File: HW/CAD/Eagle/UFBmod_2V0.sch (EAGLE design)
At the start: 75 parts, among them U301 MAX5217, U401 AT86RF215-ZU, U411 ASVTX-13-D-26.000MHZ-I05-T, U511 PE4259, U521 RFX1010, U581 B39871B3440U410, X1 TTE_EN11-HSM, X591 ANTENNATINY, X595 ANTENNATINY, X711 MOLEX 105017-0001, X721 PHOENIX_1990067_1X8X2MM50_PTS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, X722 PHOENIX_1990067_1X8X2MM50_PTS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, X723 PHOENIX_1990067_1X8X2MM50_PTS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

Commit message: HW_2V0 - HW/CAD/Eagle - board size changed
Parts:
- removed C1, C2, C3, C403, C404, C521, C531, C532, C711: 1nF, df4iah_rcl:C-EUC0402
- removed C311, C312, C406, C407, C408, C511: 100nF, df4iah_rcl:C-EUC0402
- removed C321, C401: 1uF, df4iah_rcl:C-EUC0402
- removed C411, C412, C551, C552, C553: 10nF, df4iah_rcl:C-EUC0402
- removed C413: 56pF, df4iah_rcl:C-EUC0402
- removed C591, C595, C597: 0pF, df4iah_rcl:C-EUC0402
- removed C601: 10uF, df4iah_rcl:C-EUC0603
- removed C621: 22uF, df4iah_rcl:C-EUC0603
- removed D1: ASMT-YTB7-0AA02_RGB, df4iah_led:ASMT-YTB7-0AA02_RGB
- removed H2311, H2321, H2331, H2341: MOUNT-PAD-ROUND2.8, df4iah_holes:MOUNT-PAD-ROUND2.8
- removed L1: 6.8nH, df4iah_rcl:L-EUL0603
- removed L401, L402, L403, L404: 300R, df4iah_rcl:R-EU_R1206
- removed L421: MURATA DXW21HN5011BL, df4iah_balun:DXW21HN5011BL
- removed L422: Johanson 2450BL15B050E, df4iah_balun:2450BL15B050
- removed L521: 2.7nH, df4iah_rcl:L-EUL0603
- removed L592, L596: 0nH, df4iah_rcl:L-EUL0603
- removed L611: 440nH, df4iah_rcl:L-EUL1812
- removed PF711: 1.1A/2.2A, rcl:R-EU_M1206
- removed R1, R3: 820R, df4iah_rcl:R-EU_R0402
- removed R2: 1kR, df4iah_rcl:R-EU_R0402
- removed R321: 100kR, df4iah_rcl:R-EU_R0402
- removed R4, R5, R6, R7: 10kR, df4iah_rcl:R-EU_R0402
- removed R413, R521: 100R, df4iah_rcl:R-EU_R0402
- removed R711: 330kR, df4iah_rcl:R-EU_R0402
- removed U301: MAX5217, df4iah_dac:MAX5217
- removed U401: AT86RF215-ZU, df4iah_rf:AT86RF215
- removed U411: ASVTX-13-D-26.000MHZ-I05-T, df4iah_osc:ASVTX-13-D
- removed U511: PE4259, df4iah_rf:PE4259
- removed U521: RFX1010, df4iah_rf:RFX1010
- removed U581: B39871B3440U410, df4iah_rf:B3440
- removed X1: TTE_EN11-HSM, df4iah_switch:TTE_EN11-HSM
- removed X591, X595: ANTENNATINY, _c2h:ANTENNATINY
- removed X711: MOLEX 105017-0001, df4iah_connector:USB_MICRO-B_MOLEX
- removed X721, X722, X723: PHOENIX_1990067_1X8X2MM50_PTSA-0-5, df4iah_connector:PHOENIX_1990067_1X8X2MM50_PTSA-0-5
- added C0501, C0611, C0612, C0706, C0707, C0708, C0811: 100nF, df4iah_rcl:C-EUC0402
- added C0511, C0512, C0621, C0701: 1uF, df4iah_rcl:C-EUC0402
- added C0703, C0704, C0821, C0831, C0832, C1011, C1012, C1013, C1211: 1nF, df4iah_rcl:C-EUC0402
- added C0711, C0712, C0851, C0852, C0853: 10nF, df4iah_rcl:C-EUC0402
- added C0713: 56pF, df4iah_rcl:C-EUC0402
- added C0891, C0895, C0897: 0pF, df4iah_rcl:C-EUC0402
- added C1121: 22uF, df4iah_rcl:C-EUC0603
- added D1021: ASMT-YTB7-0AA02_RGB, df4iah_led:ASMT-YTB7-0AA02_RGB
- added D1111, D1112: CRS08, df4iah_diode:CRS08
- added H1311, H1312, H1313, H1314, HB_351, HB_352, HB_353, HB_354: MOUNT-PAD-ROUND3.2, df4iah_holes:MOUNT-PAD-ROUND3.2
- added L0701, L0702, L0703, L0704: 300R, df4iah_rcl:R-EU_R1206
- added L0721: MURATA DXW21HN5011BL, df4iah_balun:DXW21HN5011BL
- added L0722: Johanson 2450BL15B050E, df4iah_balun:2450BL15B050
- added L0821: 2.7nH, df4iah_rcl:L-EUL0603
- added L0853: 6.8nH, df4iah_rcl:L-EUL0603
- added L0892, L0896: 0nH, df4iah_rcl:L-EUL0603
- added L1101: 440nH, df4iah_rcl:L-EUL1812
- added PF1211: 1.1A/2.2A, rcl:R-EU_M1206
- added R0531: 220kR, df4iah_rcl:R-EU_R0402
- added R0551: 1.5kR, df4iah_rcl:R-EU_R0402
- added R0552: 2.0kR, df4iah_rcl:R-EU_R0402
- added R0553: 27R, df4iah_rcl:R-EU_R0603
- added R0621: 100kR, df4iah_rcl:R-EU_R0402
- added R0713, R0821: 100R, df4iah_rcl:R-EU_R0402
- added R0822, R0861, R0862, R0863: 10kR, df4iah_rcl:R-EU_R0402
- added R1021, R1023: 820R, df4iah_rcl:R-EU_R0402
- added R1022: 1kR, df4iah_rcl:R-EU_R0402
- added R1211: 330kR, df4iah_rcl:R-EU_R0402
- added T0551: MMBT2222, transistor:BC846
- added U0501: MIDAS_MCCOG21605B6W-FPTLWI, df4iah_lcd:MIDAS_MCCOG21605B6W-FPTLWI
- added U0601: MAX5217, df4iah_dac:MAX5217
- added U0701: AT86RF215-ZU, df4iah_rf:AT86RF215
- added U0711: ASVTX-13-D-26.000MHZ-I05-T, df4iah_osc:ASVTX-13-D
- added U0811: PE4259, df4iah_rf:PE4259
- added U0821: RFX1010, df4iah_rf:RFX1010
- added U0881: B39871B3440U410, df4iah_rf:B3440
- added X0891, X0895: ANTENNATINY, _c2h:ANTENNATINY
- added X1011: TTE_EN11-HSM, df4iah_switch:TTE_EN11-HSM
- added X1211: MOLEX 105017-0001, df4iah_connector:USB_MICRO-B_MOLEX
- added X1221, X1222, X1223: PHOENIX_1990067_1X8X2MM50_PTSA-0-5, df4iah_connector:PHOENIX_1990067_1X8X2MM50_PTSA-0-5
- renumbered R211 to R0411, R212 to R0412
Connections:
- removed net +5V: C601.1, PF711.1
- new net +5V_USB: D1112.A, PF1211.1
- new net LCD_BL_K: T0551.C, U0501.K_BL
- new net LCD_BL_PWM: R0552.2
- new net LCD_CAP1N: C0511.2
- new net LCD_CAP1P: C0511.1
- new net LCD_NRST: R0531.2
- new net LCD_VOUT: C0512.1
- new net LED_B_B: R0551.2, R0552.1, T0551.B
- new net LED_B_E: R0553.2, T0551.E
- new net VIN_PWR: D1111.A
- new net VIN_REG: D1111.C, D1112.C
- net +3V3: now also C0501.1, C0611.1, C0612.1, C0701.1, C0711.1, C0811.1, C0851.1, C0852.1, C0853.1, C1121.1, L0703.1, L0704.1, L0853.1, L1101.1, U0501.A_BL, U0601.!AUX, U0601.REF, U0601.VDD, U0711.VCC_3V3, U0811.VDD_!CTRL, U0821.VDD1, U0821.VDD2; no longer C311.1, C312.1, C401.1, C411.1, C511.1, C551.1, C552.1, C553.1, C621.1, L1.1, L403.1, L404.1, L611.1, U301.!AUX, U301.REF, U301.VDD, U411.VCC_3V3, U511.VDD_!CTRL, U521.VDD1, U521.VDD2
- net 26MHZ_DAC_OUT: now also R0621.1, U0601.OUT; no longer R321.1, U301.OUT
- net ANT09: now also L0892.2, X0891.SIGNAL; no longer L592.2, X591.SIGNAL
- net ANT09_MATCH: now also C0891.1, L0892.1, U0881.OUT; no longer C591.1, L592.1, U581.OUT
- net ANT24: now also C0897.1, L0896.2, X0895.SIGNAL; no longer C597.1, L596.2, X595.SIGNAL
- net FE09_ANT: now also U0821.ANT, U0881.IN; no longer U521.ANT, U581.IN
- net FE09_RX: now also C0832.1, U0821.RX; no longer C532.1, U521.RX
- net FE09_TX: now also C0831.1, U0821.TX; no longer C531.1, U521.TX
- net FPGA_I2C_SCL: now also U0601.SCL; no longer U301.SCL
- net FPGA_I2C_SDA: now also U0601.SDA; no longer U301.SDA
- net FPGA_RFX_DET: now also R0821.2; no longer R521.2
- net FPGA_RFX_MODE: now also R0861.1; no longer R7.1
- net FPGA_TRX_CLKO: now also C0713.1, R0713.1; no longer C413.1, R413.1
- net GND: now also C0501.2, C0512.2, C0611.2, C0612.2, C0621.2, C0701.2, C0711.2, C0713.2, C0811.2, C0851.2, C0852.2, C0853.2, C0891.2, C0895.2, C0897.2, C1011.2, C1012.2, C1013.2, C1121.2, C1211.1, D1021.BC, D1021.GC, D1021.RC, H1311.MOUNT, H1312.MOUNT, H1313.MOUNT, H1314.MOUNT, HB_351.MOUNT, HB_352.MOUNT, HB_353.MOUNT, HB_354.MOUNT, JB1.GND@1, JB1.GND@19, JB1.GND@25, JB1.GND@30, JB1.GND@33, JB1.GND@43, JB1.GND@53, JB1.GND@54, JB1.GND@63, JB1.GND@64, JB1.GND@7, JB1.GND@73, JB1.GND@74, JB1.GND@83, JB1.GND@89, JB2.GND@19, JB2.GND@29, JB2.GND@39, JB2.GND@40, JB2.GND@49, JB2.GND@50, JB2.GND@59, JB2.GND@60, JB2.GND@69, JB2.GND@70, JB2.GND@79, JB2.GND@80, JB2.GND@89, JB3.GND@11, JB3.GND@17, JB3.GND@18, JB3.GND@23, JB3.GND@24, JB3.GND@29, JB3.GND@30, JB3.GND@35, JB3.GND@36, JB3.GND@45, JB3.GND@46, JB3.GND@5, JB3.GND@6, L0701.1, L0702.1, L0721.COM, L0722.COM, L0722.G_N_D, L0821.2, R0531.1, R0551.1, R0553.1, R0822.1, R1211.1, U0601.ADDR, U0601.GND, U0711.GND, U0811.GND, U0821.VSS@17, U0821.VSS@4, U0821.VSS@8, U0881.GROUND, X0891.GND@0, X0891.GND@1, X0891.GND@2, X0891.GND@3, X0895.GND@0, X0895.GND@1, X0895.GND@2, X0895.GND@3, X1011.C, X1011.D, X1211.GND; no longer C1.2, C2.2, C3.2, C311.2, C312.2, C321.2, C401.2, C411.2, C413.2, C511.2, C551.2, C552.2, C553.2, C591.2, C595.2, C597.2, C601.2, C621.2, C711.1, D1.BC, D1.GC, D1.RC, H2311.MOUNT, H2321.MOUNT, H2331.MOUNT, H2341.MOUNT, L401.1, L402.1, L421.COM, L422.COM, L422.G_N_D, L521.2, R6.1, R711.1, U301.ADDR, U301.GND, U411.GND, U511.GND, U521.VSS@17, U521.VSS@4, U521.VSS@8, U581.GROUND, X1.C, X1.D, X591.GND@0, X591.GND@1, X591.GND@2, X591.GND@3, X595.GND@0, X595.GND@1, X595.GND@2, X595.GND@3, X711.GND
- net LED_B1: now also R1023.2; no longer R3.2
- net LED_B_R1: now also D1021.BA, R1023.1; no longer D1.BA, R3.1
- net LED_G1: now also R1022.2; no longer R2.2
- net LED_G_R1: now also D1021.GA, R1022.1; no longer D1.GA, R2.1
- net LED_R1: now also R1021.2; no longer R1.2
- net LED_R_R1: now also D1021.RA, R1021.1; no longer D1.RA, R1.1
- net PE09_RF1: now also C0831.2, U0811.RF1; no longer C531.2, U511.RF1
- net PE09_RF2: now also C0832.2, U0811.RF2; no longer C532.2, U511.RF2
- net PE09_RFC: now also C0821.1, U0811.RFC; no longer C521.1, U511.RFC
- net PMIC3V3_SW: now also L1101.2; no longer L611.2
- net RFX_DET: now also R0821.1, R0822.2, U0821.DET; no longer R521.1, R6.2, U521.DET
- net RFX_IND: now also L0821.1, U0821.IND; no longer L521.1, U521.IND
- net RFX_MODE: now also R0861.2, U0821.MODE; no longer R7.2, U521.MODE
- net RFX_RXEN: now also R0862.2, U0821.RXEN; no longer R4.2, U521.RXEN
- net RFX_TXEN: now also R0863.2, U0821.TXEN; no longer R5.2, U521.TXEN
- net RFX_VDD3: now also L0853.2, U0821.VDD3; no longer L1.2, U521.VDD3
- net ROT_I_R: now also C1011.1, X1011.A; no longer C1.1, X1.A
- net ROT_P: now also C1013.1, X1011.E; no longer C3.1, X1.E
- net ROT_Q_R: now also C1012.1, X1011.B; no longer C2.1, X1.B
- net TRX_AVDD0: now also C0707.2, U0701.AVDD0; no longer C407.2, U401.AVDD0
- net TRX_AVDD1: now also C0708.2, U0701.AVDD1; no longer C408.2, U401.AVDD1
- net TRX_AVSS: now also C0704.2, C0707.1, C0708.1, L0701.2, U0701.AVSS, U0701.XTAL2; no longer C404.2, C407.1, C408.1, L401.2, U401.AVSS, U401.XTAL2
- net TRX_CLKO: now also R0713.2, U0701.CLKO; no longer R413.2, U401.CLKO
- net TRX_DEVDD: now also C0703.1, L0703.2, U0701.DEVDD; no longer C403.1, L403.2, U401.DEVDD
- net TRX_DVDD: now also C0706.2, U0701.DVDD; no longer C406.2, U401.DVDD
- net TRX_DVSS: now also C0703.2, C0706.1, L0702.2, U0701.DVSS; no longer C403.2, C406.1, L402.2, U401.DVSS
- net TRX_EVDD: now also C0704.1, L0704.2, U0701.EVDD; no longer C404.1, L404.2, U401.EVDD
- net TRX_FEA09: now also R0863.1, U0701.FEA09, U0811.CTRL; no longer R5.1, U401.FEA09, U511.CTRL
- net TRX_FEA24: now also U0701.FEA24; no longer U401.FEA24
- net TRX_FEB09: now also R0862.1, U0701.FEB09; no longer R4.1, U401.FEB09
- net TRX_FEB24: now also U0701.FEB24; no longer U401.FEB24
- net TRX_IRQ: now also U0701.IRQ; no longer U401.IRQ
- net TRX_MISO: now also U0701.MISO; no longer U401.MISO
- net TRX_MOSI: now also U0701.MOSI; no longer U401.MOSI
- net TRX_RF09: now also C0821.2, L0721.UB; no longer C521.2, L421.UB
- net TRX_RF09_N: now also L0721.B2, U0701.RF09N; no longer L421.B2, U401.RF09N
- net TRX_RF09_P: now also L0721.B1, U0701.RF09P; no longer L421.B1, U401.RF09P
- net TRX_RF24: now also C0895.1, L0722.UB, L0896.1; no longer C595.1, L422.UB, L596.1
- net TRX_RF24_N: now also L0722.B2, U0701.RF24N; no longer L422.B2, U401.RF24N
- net TRX_RF24_P: now also L0722.B1, U0701.RF24P; no longer L422.B1, U401.RF24P
- net TRX_RSTN: now also U0701.RSTN; no longer U401.RSTN
- net TRX_RXCLK_N: now also U0701.RXCLKN; no longer U401.RXCLKN
- net TRX_RXCLK_P: now also U0701.RXCLKP; no longer U401.RXCLKP
- net TRX_RXD09_N: now also U0701.RXD09N; no longer U401.RXD09N
- net TRX_RXD09_P: now also U0701.RXD09P; no longer U401.RXD09P
- net TRX_RXD24_N: now also U0701.RXD24N; no longer U401.RXD24N
- net TRX_RXD24_P: now also U0701.RXD24P; no longer U401.RXD24P
- net TRX_SCLK: now also U0701.SCLK; no longer U401.SCLK
- net TRX_SELN: now also U0701.SELN; no longer U401.SELN
- net TRX_TCXO: now also C0712.2, U0701.TCXO; no longer C412.2, U401.TCXO
- net TRX_TXCLK_N: now also U0701.TXCLKN; no longer U401.TXCLKN
- net TRX_TXCLK_P: now also U0701.TXCLKP; no longer U401.TXCLKP
- net TRX_TXD_N: now also U0701.TXDN; no longer U401.TXDN
- net TRX_TXD_P: now also U0701.TXDP; no longer U401.TXDP
- net USB_SHIELD: now also C1211.2, R1211.2, X1211.SHIELD; no longer C711.2, R711.2, X711.SHIELD
- net USB_VBUS: now also PF1211.2, X1211.J_VUSB; no longer PF711.2, X711.J_VUSB
- net VCTCXO_OUT: now also C0712.1, U0711.OUT; no longer C412.1, U411.OUT
- net VCTCXO_VC: now also C0621.1, R0621.2, U0711.VC; no longer C321.1, R321.2, U411.VC
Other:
- note added: "Addr Device 0x38 DAC 0x3D LCD"
- note added: "I2C LCD module I2C addr: 0x3D"
- note added: "I2C: LCD"
- note added: "LCD_NRST"
- note added: "Module mount pads"
- note added: "X0891"
- note added: "X0895"
- note removed: "Addr Device 0x38 DAC"
- note removed: "X591"
- note removed: "X595"

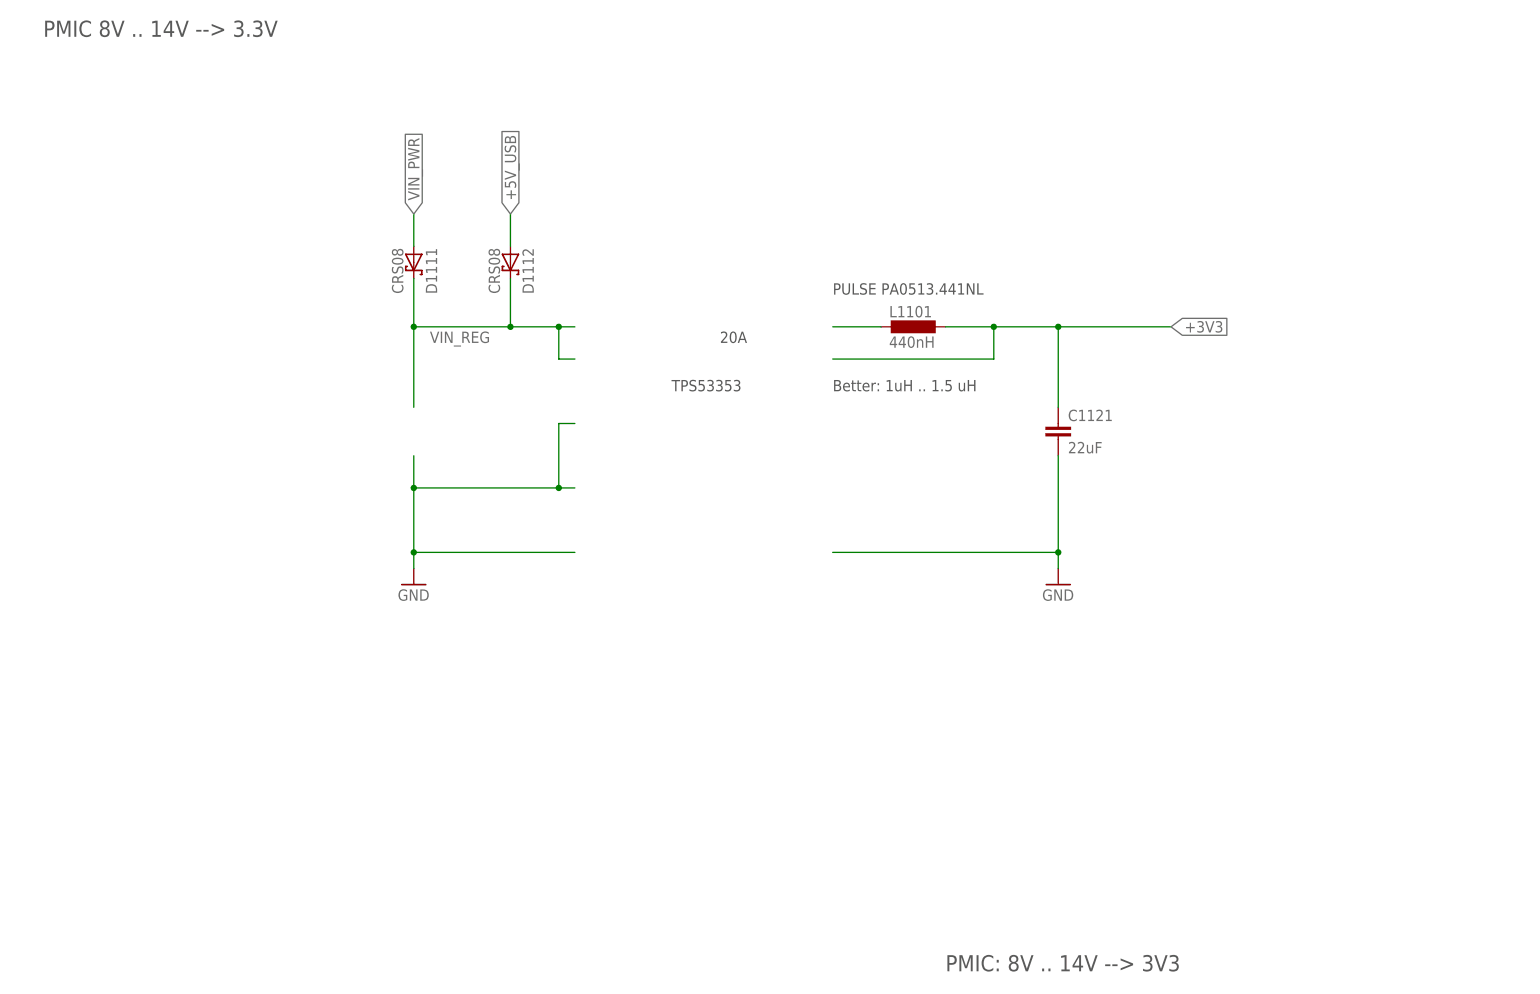
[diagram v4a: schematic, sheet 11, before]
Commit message: HW_2V0 - HW/CAD/Eagle - TPS53353 added
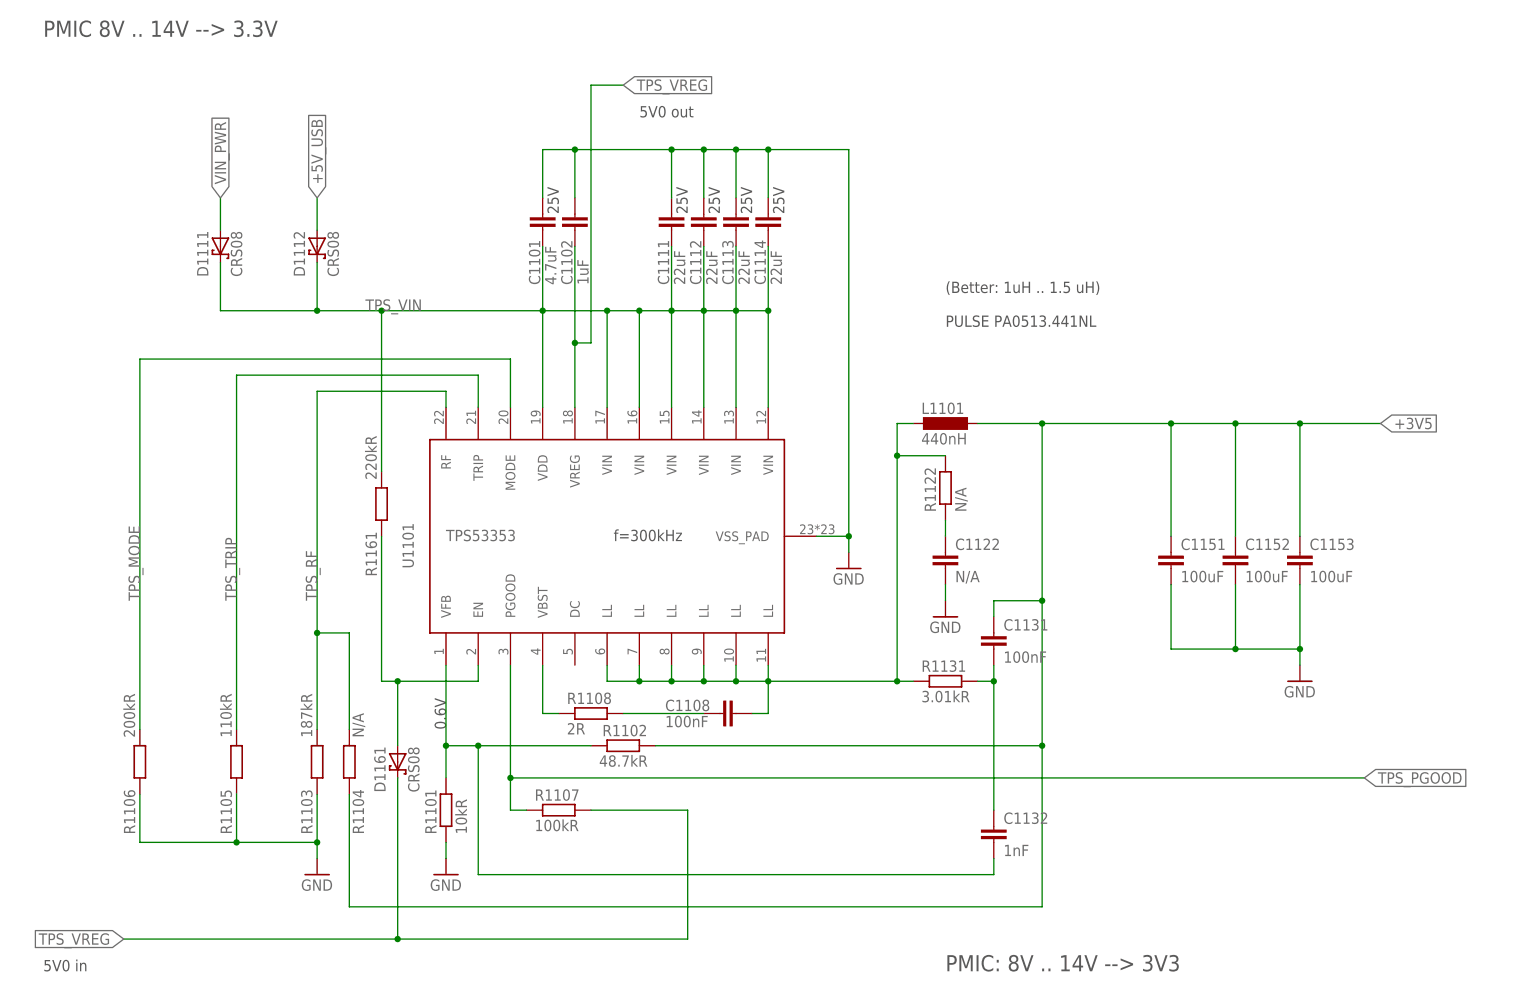
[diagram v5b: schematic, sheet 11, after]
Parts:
- removed C1121: 22uF, df4iah_rcl:C-EUC0603
- added C1101: 4.7uF, df4iah_rcl:C-EUC0805
- added C1102: 1uF, df4iah_rcl:C-EUC0402
- added C1108: 100nF, df4iah_rcl:C-EUC0805
- added C1111, C1112, C1113, C1114: 22uF, df4iah_rcl:C-EUC0805
- added C1122: N/A, df4iah_rcl:C-EUC0805
- added C1131: 100nF, df4iah_rcl:C-EUC0402
- added C1132: 1nF, df4iah_rcl:C-EUC0402
- added C1151, C1152, C1153: 100uF, df4iah_rcl:C-EUC0805
- added D1161: CRS08, df4iah_diode:CRS08
- added R1101: 10kR, df4iah_rcl:R-EU_R0402
- added R1102: 48.7kR, df4iah_rcl:R-EU_R0402
- added R1103: 187kR, df4iah_rcl:R-EU_R0402
- added R1104: N/A, df4iah_rcl:R-EU_R0402
- added R1105: 110kR, df4iah_rcl:R-EU_R0402
- added R1106: 200kR, df4iah_rcl:R-EU_R0402
- added R1107: 100kR, df4iah_rcl:R-EU_R0402
- added R1108: 2R, df4iah_rcl:R-EU_R0805
- added R1122: N/A, df4iah_rcl:R-EU_R0805
- added R1131: 3.01kR, df4iah_rcl:R-EU_R0402
- added R1161: 220kR, df4iah_rcl:R-EU_R0402
- added U1101: TPS53353, df4iah_powersupply:TPS53353
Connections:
- removed net PMIC3V3_SW: L1101.2
- removed net VIN_REG: D1111.C, D1112.C
- new net +3V5: C1131.1, C1151.1, C1152.1, C1153.1, L1101.1, R1102.2, R1104.1
- new net TPS_COR: C1131.2, C1132.1, R1131.2
- new net TPS_EN: D1161.A, R1161.1, U1101.EN
- new net TPS_LL: C1108.1, L1101.2, R1122.2, R1131.1, U1101.LL@10, U1101.LL@11, U1101.LL@6, U1101.LL@7, U1101.LL@8, U1101.LL@9
- new net TPS_LL_RC: C1122.1, R1122.1
- new net TPS_MODE: R1106.2, U1101.MODE
- new net TPS_PGOOD: R1107.1, U1101.PGOOD
- new net TPS_RF: R1103.2, R1104.2, U1101.RF
- new net TPS_TRIP: R1105.2, U1101.TRIP
- new net TPS_VBST: R1108.1, U1101.VBST
- new net TPS_VBST_R: C1108.2, R1108.2
- new net TPS_VFB: C1132.2, R1101.2, R1102.1, U1101.VFB
- new net TPS_VIN: C1101.2, C1111.2, C1112.2, C1113.2, C1114.2, D1111.C, D1112.C, R1161.2, U1101.VDD, U1101.VIN@12, U1101.VIN@13, U1101.VIN@14, U1101.VIN@15, U1101.VIN@16, U1101.VIN@17
- new net TPS_VREG: C1102.2, D1161.C, R1107.2, U1101.VREG
- net +3V3: no longer C1121.1, L1101.1
- net GND: now also C1101.1, C1102.1, C1111.1, C1112.1, C1113.1, C1114.1, C1122.2, C1151.2, C1152.2, C1153.2, R1101.1, R1103.1, R1105.1, R1106.1, U1101.VSS_PAD; no longer C1121.2
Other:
- note added: "(Better: 1uH .. 1.5 uH)"
- note added: "0.6V"
- note added: "25V"
- note added: "5V0 in"
- note added: "5V0 out"
- note added: "f=300kHz"
- note removed: "20A"
- note removed: "Better: 1uH .. 1.5 uH"
- note removed: "TPS53353"
- moved on the sheet: D1111, D1112, L1101

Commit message: HW_2V0 - HW/CAD/Eagle - work of the day
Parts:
- removed C1211: 1nF, df4iah_rcl:C-EUC0402
- removed H1311, H1312, H1313, H1314: MOUNT-PAD-ROUND3.2, df4iah_holes:MOUNT-PAD-ROUND3.2
- removed PF1211: 1.1A/2.2A, rcl:R-EU_M1206
- removed R1211: 330kR, df4iah_rcl:R-EU_R0402
- removed X1211: MOLEX 105017-0001, df4iah_connector:USB_MICRO-B_MOLEX
- removed X1221, X1222, X1223: PHOENIX_1990067_1X8X2MM50_PTSA-0-5, df4iah_connector:PHOENIX_1990067_1X8X2MM50_PTSA-0-5
- added C1201, C1221: 10uF, df4iah_rcl:C-EUC0603
- added C1311: 1nF, df4iah_rcl:C-EUC0402
- added H1411, H1412, H1413, H1414: MOUNT-PAD-ROUND3.2, df4iah_holes:MOUNT-PAD-ROUND3.2
- added L1211: 4.7uH, df4iah_rcl:L-EUL2520
- added PF1311: 1.1A/2.2A, rcl:R-EU_M1206
- added R0001, R0002, R0003, R0532: 1kR, df4iah_rcl:R-EU_R0402
- added R0211: 0R, df4iah_rcl:R-EU_R0402
- added R0212: N/A, df4iah_rcl:R-EU_R0402
- added R1311: 330kR, df4iah_rcl:R-EU_R0402
- added U1211: TPS62745DSSR, df4iah_powersupply:TPS62745
- added X1311: MOLEX 105017-0001, df4iah_connector:USB_MICRO-B_MOLEX
- added X1321, X1322, X1323: PHOENIX_1990067_1X8X2MM50_PTSA-0-5, df4iah_connector:PHOENIX_1990067_1X8X2MM50_PTSA-0-5
- C1011, C1012, C1013: value 1nF -> 100nF
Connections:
- net LCD_BL_PWM renamed FPGA_LCD_BL_PWM
- net LED_B1 renamed FPGA_LED_RGB_BLUE
- net LED_B_B renamed LCD_BL_B
- net LED_B_R1 renamed LED_RGB_BLUE
- net LED_G1 renamed FPGA_LED_RGB_GREEN
- net LED_G_R1 renamed LED_RGB_GREEN
- net LED_R1 renamed FPGA_LED_RGB_RED
- net LED_R_R1 renamed LED_RGB_RED
- removed net ROT_I_R: C1011.1, X1011.A
- removed net ROT_Q_R: C1012.1, X1011.B
- new net +1V5: JB2.U1V5@20
- new net +1V8: JB1.U1V8@40, R0212.1
- new net +2V5: C1221.1, L1211.1, R0211.1, U1211.VOUT
- new net FPGA_ETH_RD_N: JB1.ETH_RD_N
- new net FPGA_ETH_RD_P: JB1.ETH_RD_P
- new net FPGA_ETH_TD_N: JB1.ETH_TD_N
- new net FPGA_ETH_TD_P: JB1.ETH_TD_P
- new net FPGA_LCD_NRST: R0532.1
- new net FPGA_ROT_I: R0001.2
- new net FPGA_ROT_P: R0003.2
- new net FPGA_ROT_Q: R0002.2
- new net PMIC3V3_SW: L1211.2, U1211.SW
- new net ROT_I: C1011.1, R0001.1, X1011.A
- new net ROT_Q: C1012.1, R0002.1, X1011.B
- new net VCCIO13: JB2.VCCIO13@2, JB2.VCCIO13@4, R0211.2, R0212.2
- net +3V3: now also JB1.U3V3@13, JB1.VCCIO16@10, JB1.VCCIO16@12, JB2.U3V3@11, JB2.U3V3@9, JB2.VCCIO15@10, JB2.VCCIO15@8, U0501.VDD
- net +3V5: now also C1201.1, JB1.U3V3IN@14, JB1.U3V3IN@16, JB1.VIN@2, JB1.VIN@4, JB1.VIN@6, JB2.VIN@1, JB2.VIN@3, JB2.VIN@5, JB2.VIN@7, U1211.EN, U1211.VIN, U1211.VSEL1, U1211.VSEL2, U1211.VSEL3
- net +5V_USB: now also PF1311.1; no longer PF1211.1
- net FPGA_I2C_SCL: now also U0501.SCL
- net FPGA_I2C_SDA: now also U0501.SDA
- net GND: now also C1201.2, C1221.2, C1311.1, H1411.MOUNT, H1412.MOUNT, H1413.MOUNT, H1414.MOUNT, R1311.1, U0501.VSS, U1211.EN_VIN_SW, U1211.VSEL4, U1211.VSS, X1311.GND, X1323.8; no longer C1211.1, H1311.MOUNT, H1312.MOUNT, H1313.MOUNT, H1314.MOUNT, R1211.1, X1211.GND
- net LCD_CAP1N: now also U0501.CAP1N
- net LCD_CAP1P: now also U0501.CAP1P
- net LCD_NRST: now also R0532.2, U0501.RST
- net LCD_VOUT: now also U0501.VOUT
- net ROT_P: now also R0003.1
- net USB_SHIELD: now also C1311.2, R1311.2, X1311.SHIELD; no longer C1211.2, R1211.2, X1211.SHIELD
- net USB_VBUS: now also PF1311.2, X1311.J_VUSB; no longer PF1211.2, X1211.J_VUSB
- net VIN_PWR: now also X1323.7
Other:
- note added: "300mA"
- note added: "Board-Wire-Connectors"
- note added: "JTAG-Connector"
- note added: "MURATA DFE252010P-4R7M=P2"
- note added: "PMIC 3.5V --> 2.5V"
- note added: "PMIC 5V..14V --> 3.5V"
- note added: "PMIC: 3.5V --> 2.5V"
- note added: "PMIC: 5V..14V --> 3.5V"
- note added: "Prog: 2.5V"
- note added: "USB-Connector"
- note added: "Xilinx JTAG header. Dual row, 2mm, 14 pin, shrouded. SULLINS CONNECTOR SOLUTIONS SBH21-NBPN-D07-ST-BK"
- note removed: "LCD_NRST"
- note removed: "PMIC 8V .. 14V --> 3.3V"
- note removed: "PMIC: 8V .. 14V --> 3V3"

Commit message: HW_2V0 - HW/CAD/Eagle - XILINX-JTAG header added, some more placements done
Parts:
- removed R0001, R0002, R0003: 1kR, df4iah_rcl:R-EU_R0402
- removed R0212: N/A, df4iah_rcl:R-EU_R0402
- added R0202: N/A, df4iah_rcl:R-EU_R0402
- added R1011, R1012, R1013, R1331: 1kR, df4iah_rcl:R-EU_R0402
- added R1211, R1338: 10kR, df4iah_rcl:R-EU_R0402
- added R1332, R1333, R1334, R1335, R1337, R1339: 100R, df4iah_rcl:R-EU_R0402
- added X1331: (no value), df4iah_connector:XILINX-JTAG-14
- added X1332: (no value), df4iah_connector:HEADER-1X2
- R1101: value 10kR -> 10kR 0%5
- R1102: value 48.7kR -> 45.3kR 0%5
- renumbered R0211 to R0201
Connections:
- net +1V5 renamed U1V5
- removed net +1V8: JB1.U1V8@40, R0212.1
- removed net +3V5: C1131.1, C1151.1, C1152.1, C1153.1, C1201.1, JB1.U3V3IN@14, JB1.U3V3IN@16, JB1.VIN@2, JB1.VIN@4, JB1.VIN@6, JB2.VIN@1, JB2.VIN@3, JB2.VIN@5, JB2.VIN@7, L1101.1, R1102.2, R1104.1, U1211.EN, U1211.VIN, U1211.VSEL1, U1211.VSEL2, U1211.VSEL3
- new net FPGA_JTAGEN: JB1.JTAGEN@90, R1339.2
- new net FPGA_SRST: JB2.B15_IO0, R1337.2
- new net FPGA_TCK: JB2.TCK, R1333.2
- new net FPGA_TDI: JB2.TDI, R1335.2
- new net FPGA_TDO: JB2.TDO, R1334.2
- new net FPGA_TMS: JB2.TMS, R1332.2
- new net JC_SRST: R1337.1, X1331.14
- new net JC_TCK: R1333.1, X1331.6
- new net JC_TDI: R1335.1, X1331.10
- new net JC_TDO: R1334.1, X1331.8
- new net JC_TMS: R1332.1, X1331.4
- new net JC_VCCO_0: R1331.1, X1331.2
- new net JTAG_CPLD_EN: R1338.1, R1339.1, X1332.2
- new net TPS2_EN: R1211.2, U1211.EN
- new net U1V8: JB1.U1V8@40, R0202.1
- new net U3V3: JB1.U3V3@13, JB1.VCCIO16@10, JB1.VCCIO16@12, JB2.U3V3@11, JB2.U3V3@9, JB2.VCCIO15@10, JB2.VCCIO15@8, R1211.1
- new net U3V3_JTAGREF: JB2.U3V3_JTAGREF, R1331.2
- new net USB_D_M: X1311.J_D-
- new net USB_D_P: X1311.J_D+
- new net USB_ID: X1311.J_ID
- net +3V3: now also C1131.1, C1151.1, C1152.1, C1153.1, C1201.1, JB1.U3V3IN@14, JB1.U3V3IN@16, JB1.VIN@2, JB1.VIN@4, JB1.VIN@6, JB2.VIN@1, JB2.VIN@3, JB2.VIN@5, JB2.VIN@7, L1101.1, R1102.2, R1104.1, U1211.VIN, U1211.VSEL1, U1211.VSEL2, U1211.VSEL3, X1332.1; no longer JB1.U3V3@13, JB1.VCCIO16@10, JB1.VCCIO16@12, JB2.U3V3@11, JB2.U3V3@9, JB2.VCCIO15@10, JB2.VCCIO15@8
- net FPGA_ROT_I: now also R1011.2; no longer R0001.2
- net FPGA_ROT_P: now also R1013.2; no longer R0003.2
- net FPGA_ROT_Q: now also R1012.2; no longer R0002.2
- net FPGA_TRX_CLKO: now also JB1.B16_L12_CLK_P
- net GND: now also R1338.2, X1331.1, X1331.11, X1331.13, X1331.3, X1331.5, X1331.7, X1331.9
- net ROT_I: now also R1011.1; no longer R0001.1
- net ROT_P: now also R1013.1; no longer R0003.1
- net ROT_Q: now also R1012.1; no longer R0002.1
- net TRX_RXCLK_N: now also JB1.B13_L11_N
- net TRX_RXCLK_P: now also JB1.B13_L11_P
- net TRX_RXD09_N: now also JB1.B13_L3_N
- net TRX_RXD09_P: now also JB1.B13_L3_P
- net TRX_RXD24_N: now also JB1.B13_L9_N
- net TRX_RXD24_P: now also JB1.B13_L9_P
- net TRX_TXCLK_N: now also JB1.B13_L6_N
- net TRX_TXCLK_P: now also JB1.B13_L6_P
- net TRX_TXD_N: now also JB1.B13_L5_N
- net TRX_TXD_P: now also JB1.B13_L5_P
- net VCCIO13: now also R0202.2; no longer R0212.2
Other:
- note added: "JTAG CPLD EN"
- note added: "PMIC 5V..14V --> 3.3V_REG"
- note added: "PMIC: 5V..14V --> 3.3V"
- note removed: "PMIC 5V..14V --> 3.5V"
- note removed: "PMIC: 5V..14V --> 3.5V"
- note removed: "Xilinx JTAG header. Dual row, 2mm, 14 pin, shrouded. SULLINS CONNECTOR SOLUTIONS SBH21-NBPN-D07-ST-BK"
